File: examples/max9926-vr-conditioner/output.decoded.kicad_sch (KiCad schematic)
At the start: 10 parts, among them IC16 MAX9926UAEE_V+

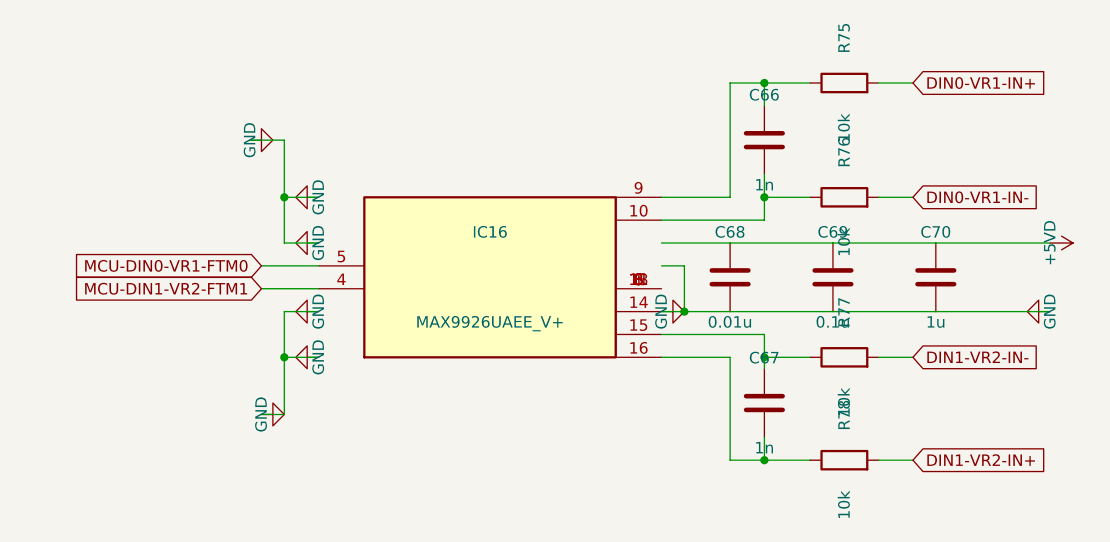
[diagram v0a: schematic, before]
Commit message: Add footprint lookup table for TOKN decoder
- Add footprints.json with comprehensive lookup table:
  - Common passive sizes (0402, 0603, 0805, etc.)
  - IC packages (SOIC, TSSOP, QFN, LQFP, etc.)
  - Specific parts (MCP2551, MAX232, ATmega, STM32, etc.)
  - Transistors, regulators, op-amps, and more

- Update tokn_decoder.py to auto-populate footprints:
  - Priority: explicit > package hint > part match > passive type
  - Handles size codes (0603) for passives automatically

Decoded schematics now have proper footprints ready for PCB layout.
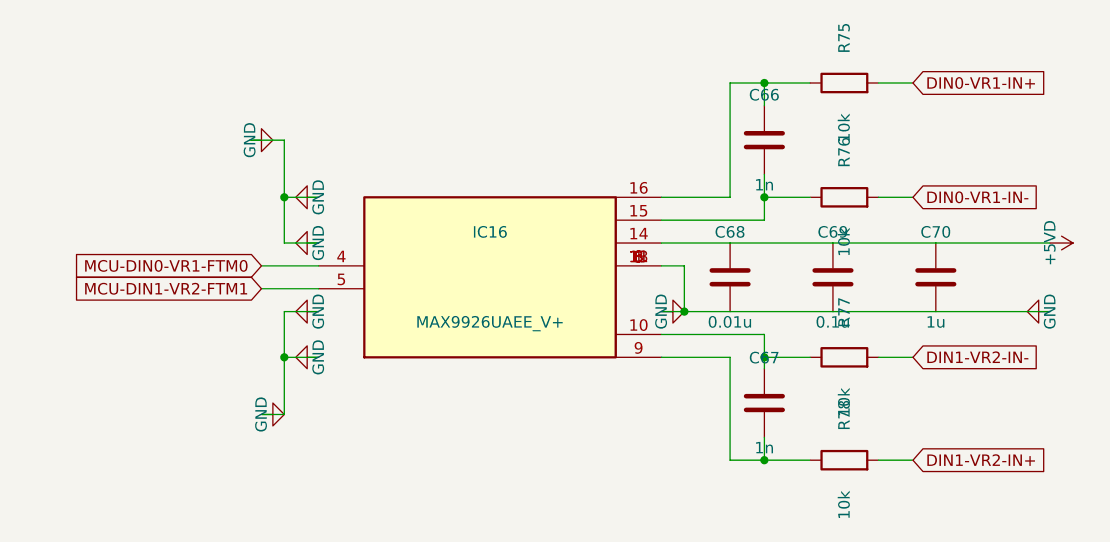
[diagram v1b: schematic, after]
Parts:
- C66, C67, C68, C69, C70: footprint (none) -> Capacitor_SMD:C_0603_1608Metric
- IC16: footprint SOP64P602X175-16N -> Package_SO:TSSOP-14_4.4x5mm_P0.65mm
- R75, R76, R77, R78: footprint 0603 -> Resistor_SMD:R_0603_1608Metric
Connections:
- net +5VD: now also IC16.14
- net GND: now also IC16.1, IC16.11, IC16.13, IC16.3, IC16.6, IC16.8; no longer IC16.14
- net MCU-DIN0-VR1-FTM0: now also IC16.4; no longer IC16.5
- net MCU-DIN1-VR2-FTM1: now also IC16.5; no longer IC16.4
- net at C67.1, R77.1: now also IC16.10; no longer IC16.15
- net at C66.2, R76.1: now also IC16.15; no longer IC16.10
- net at C67.2, R78.1: now also IC16.9; no longer IC16.16
- net at C66.1, R75.1: now also IC16.16; no longer IC16.9
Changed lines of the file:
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@@
       (at 160.02 78.66 0)
       (effects (font (size 1.27 1.27))))
-    (property "Footprint" ""
+    (property "Footprint" "Capacitor_SMD:C_0603_1608Metric"
       (at 160.02 73.66 0)
       (effects (font (size 1.27 1.27)) (hide yes)))
@@
       (at 160.02 107.87 0)
       (effects (font (size 1.27 1.27))))
-    (property "Footprint" ""
+    (property "Footprint" "Capacitor_SMD:C_0603_1608Metric"
       (at 160.02 102.87 0)
       (effects (font (size 1.27 1.27)) (hide yes)))
@@
       (at 156.21 93.9 0)
       (effects (font (size 1.27 1.27))))
-    (property "Footprint" ""
+    (property "Footprint" "Capacitor_SMD:C_0603_1608Metric"
       (at 156.21 88.9 0)
       (effects (font (size 1.27 1.27)) (hide yes)))
@@
       (at 167.64 93.9 0)
       (effects (font (size 1.27 1.27))))
-    (property "Footprint" ""
+    (property "Footprint" "Capacitor_SMD:C_0603_1608Metric"
       (at 167.64 88.9 0)
       (effects (font (size 1.27 1.27)) (hide yes)))
@@
       (at 179.07 93.9 0)
       (effects (font (size 1.27 1.27))))
-    (property "Footprint" ""
+    (property "Footprint" "Capacitor_SMD:C_0603_1608Metric"
       (at 179.07 88.9 0)
       (effects (font (size 1.27 1.27)) (hide yes)))
@@
       (at 129.54 93.9 0)
       (effects (font (size 1.27 1.27))))
-    (property "Footprint" "SOP64P602X175-16N"
+    (property "Footprint" "Package_SO:TSSOP-14_4.4x5mm_P0.65mm"
       (at 129.54 88.9 0)
       (effects (font (size 1.27 1.27)) (hide yes)))
@@
       (at 168.91 72.31 0)
       (effects (font (size 1.27 1.27))))
-    (property "Footprint" "0603"
+    (property "Footprint" "Resistor_SMD:R_0603_1608Metric"
       (at 168.91 67.31 0)
       (effects (font (size 1.27 1.27)) (hide yes)))
@@
       (at 168.91 85.01 0)
       (effects (font (size 1.27 1.27))))
-    (property "Footprint" "0603"
+    (property "Footprint" "Resistor_SMD:R_0603_1608Metric"
       (at 168.91 80.01 0)
       (effects (font (size 1.27 1.27)) (hide yes)))
@@
       (at 168.91 102.79 0)
       (effects (font (size 1.27 1.27))))
-    (property "Footprint" "0603"
+    (property "Footprint" "Resistor_SMD:R_0603_1608Metric"
       (at 168.91 97.79 0)
       (effects (font (size 1.27 1.27)) (hide yes)))
@@
       (at 168.91 114.22 0)
       (effects (font (size 1.27 1.27))))
-    (property "Footprint" "0603"
+    (property "Footprint" "Resistor_SMD:R_0603_1608Metric"
       (at 168.91 109.22 0)
       (effects (font (size 1.27 1.27)) (hide yes)))

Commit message: Fix decoder pin placement using TOKN pins section
- Use pin definitions from TOKN pins{REF}[N]: section instead of
  deriving positions from wire endpoints
- Calculate pin positions using standard dual-inline IC layout:
  pins 1-N/2 on left (top to bottom), N/2+1 to N on right (bottom to top)
- Include pin names from TOKN in generated lib_symbols
- Fix issue where pins with same net were merged to same position
- Regenerate all decoded schematics with correct pin placement
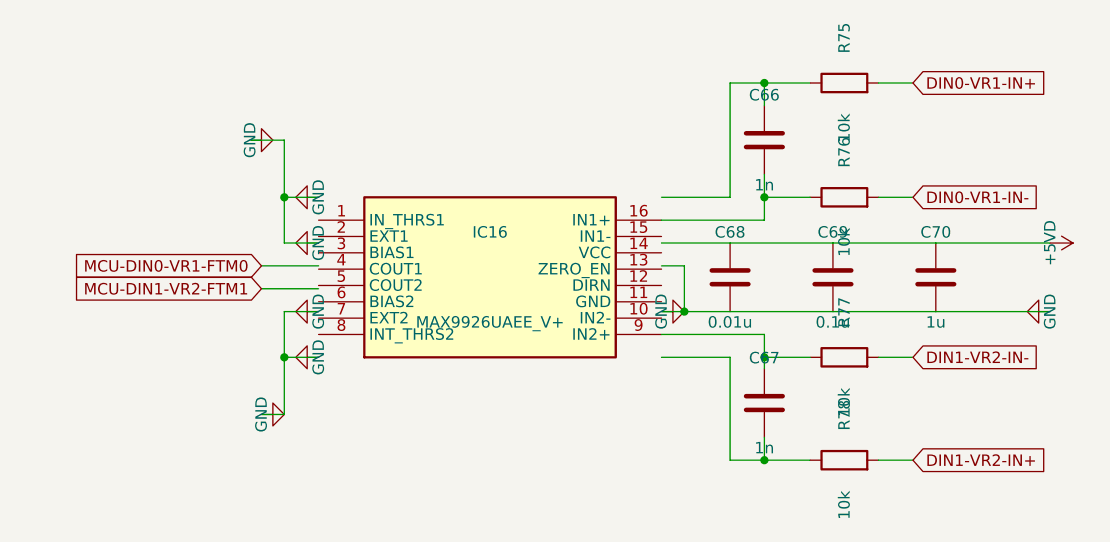
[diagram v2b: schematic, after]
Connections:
- net +5VD: no longer IC16.14
- net GND: no longer IC16.1, IC16.11, IC16.13, IC16.3, IC16.6, IC16.8
- net MCU-DIN0-VR1-FTM0: no longer IC16.4
- net MCU-DIN1-VR2-FTM1: no longer IC16.5
- net at C67.1, R77.1: now also IC16.9 (IN2+); no longer IC16.10
- net at C66.2, R76.1: now also IC16.16 (IN1+); no longer IC16.15
- net at C66.1, R75.1: no longer IC16.16
- net at C67.2, R78.1: no longer IC16.9
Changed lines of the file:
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@@
       (at 129.54 88.9 0)
       (effects (font (size 1.27 1.27)) (hide yes)))
-    (pin "14"
-    )
     (pin "1"
     )
+    (pin "2"
+    )
     (pin "3"
-    )
-    (pin "6"
-    )
-    (pin "8"
-    )
-    (pin "11"
-    )
-    (pin "13"
     )
     (pin "4"
@@
     (pin "5"
     )
+    (pin "6"
+    )
+    (pin "7"
+    )
+    (pin "8"
+    )
     (pin "9"
+    )
+    (pin "10"
+    )
+    (pin "11"
+    )
+    (pin "12"
+    )
+    (pin "13"
+    )
+    (pin "14"
+    )
+    (pin "15"
     )
     (pin "16"
     )
-    (pin "15"
-    )
-    (pin "10"
-    )
     (instances
